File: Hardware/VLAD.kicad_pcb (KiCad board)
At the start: 2 copper layers, 90 x 80 mm, 100 parts, among them J1 BMP388, J2 BNO055, J3 Micro_SD_Card, J4 Conn_01x02_Male, J5 Conn_01x03_Male, J6 Conn_01x02_Male, P1 USB_C_Plug_USB2.0, Q1 MMDT2222A, Q2 MMDT2222A, Q3 S8550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

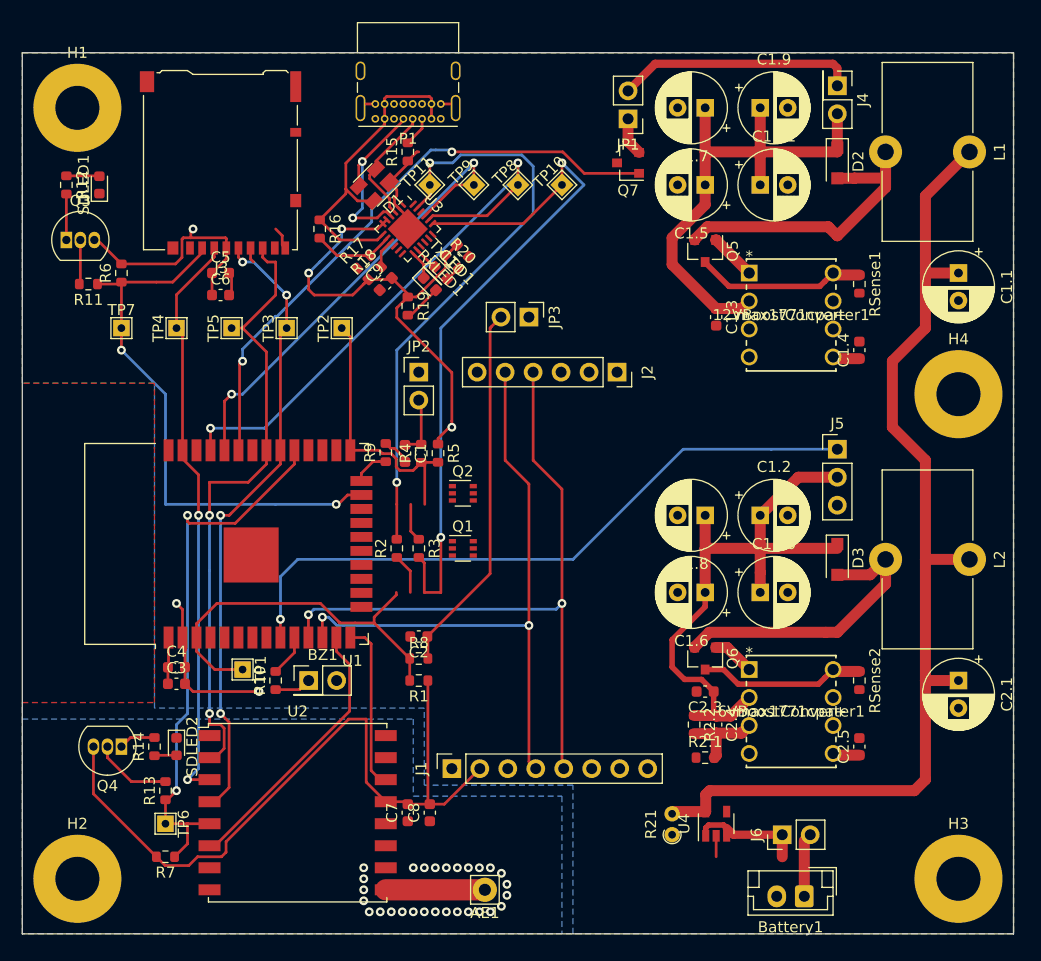
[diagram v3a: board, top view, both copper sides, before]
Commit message: Executive decision to use THT capacitors
THT >>>>>>>>>>>> SMD
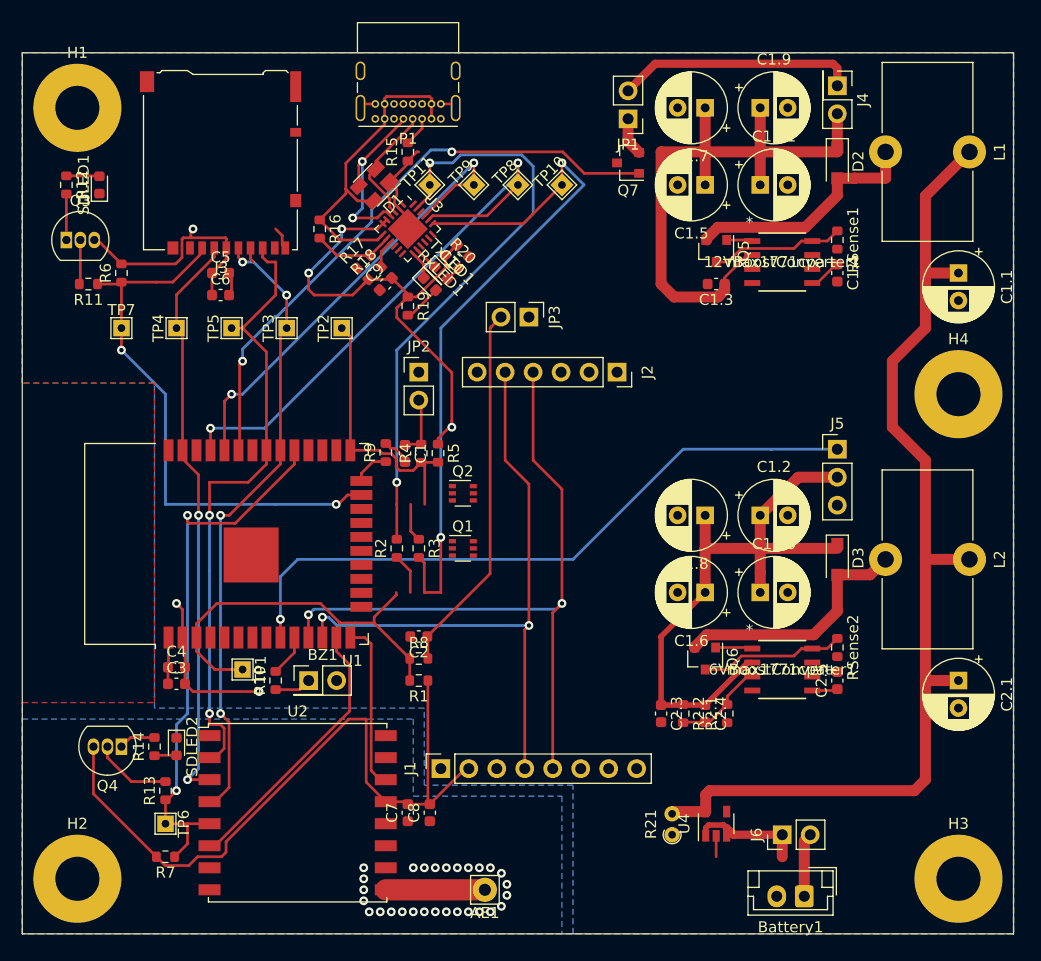
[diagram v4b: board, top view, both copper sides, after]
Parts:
- 12VBoostConverter1, 6VBoostConverter1: footprint footprints:max1771cpa&plus_ -> iclr:MAX1771CSA&plus_
- moved C1.4 7.28 mm to (94.0, 40.0), turned to 270 degrees
- moved C2.5 6.32 mm to (94.0, 77.0)
- moved C2.3 4.47 mm to (78.0, 80.0), turned to 270 degrees
- moved R2.1 4.47 mm to (84.0, 80.0), turned to 90 degrees
- moved RSense1 4.47 mm to (94.0, 37.0)
- moved RSense2 3.61 mm to (94.0, 74.0)
- moved 12VBoostConverter1 3.16 mm to (89.0, 39.0)
- moved 6VBoostConverter1 3.00 mm to (89.0, 76.0)
- moved C1.3 3.00 mm to (83.0, 41.0), turned to 180 degrees
- moved C2.4 1.41 mm to (82.0, 80.0)
- moved R2.2 1.41 mm to (80.0, 80.0)
- moved J1 1.00 mm to (58.0, 85.0)
- moved Q5 1.00 mm to (83.0, 38.0)
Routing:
- net +12V: track 46.9 -> 56.5 mm
- net Net-(D2-Pad2): track 27.6 -> 22.0 mm
- net Net-(D3-Pad2): track 26.9 -> 22.6 mm
- net Net-(12VBoostConverter1-Pad8): track 15.5 -> 12.2 mm
- net Net-(6VBoostConverter1-Pad8): track 15.2 -> 13.2 mm
- net Net-(12VBoostConverter1-Pad1): track 4.29 -> 2.37 mm
- net +6V: track 55.2 -> 56.2 mm
- net +3V3: track 150.0 -> 149.0 mm
- net Net-(12VBoostConverter1-Pad5): track 2.44 -> 2.97 mm
- net Net-(6VBoostConverter1-Pad1): track 3.88 -> 3.37 mm

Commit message: Traccs done, meme time
Need to fix the silkscreen stuff for the components and also the back silkscreen memes etc.
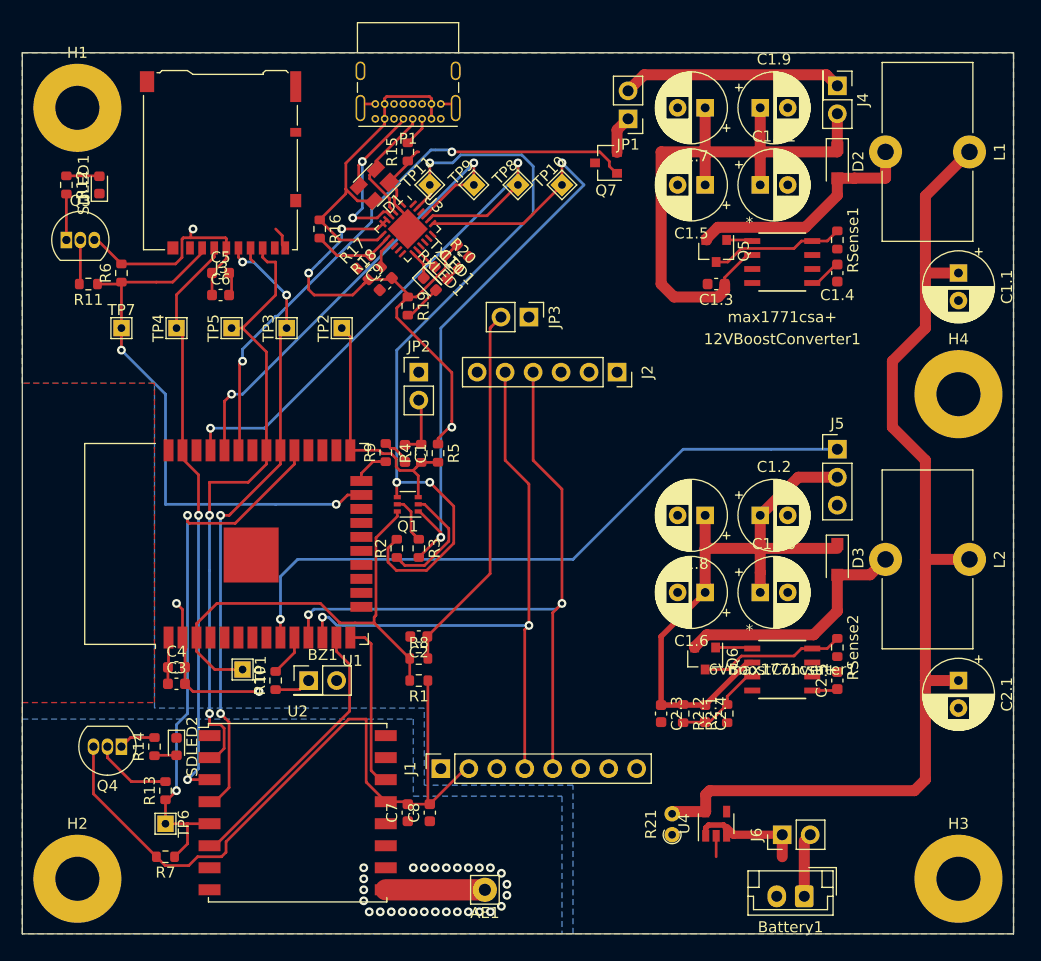
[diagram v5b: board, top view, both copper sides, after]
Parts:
- removed Q2: MMDT2222A, Package_TO_SOT_SMD:SOT-363_SC-70-6
- 12VBoostConverter1, 6VBoostConverter1: value max1771cpa+ -> max1771csa+
- moved Q1 6.40 mm to (55.0, 61.0), turned to 180 degrees
- moved Q7 2.00 mm to (73.0, 30.0)
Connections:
- Q1 pad 1: /EN -> /USB_RTS
- Q1 pad 3: (no net) -> /IO0
- Q1 pad 4: (no net) -> /USB_DTR
- Q1 pad 5: (no net) -> Net-(Q1-Pad5)
- Q1 pad 6: /USB_RTS -> /EN
- R3 pad 1: Net-(Q2-Pad2) -> Net-(Q1-Pad5)
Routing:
- net /USB_DTR: track 53.7 -> 69.0 mm, vias 2 -> 3
- net /EN: track 36.1 -> 43.5 mm
- net Net-(Q1-Pad2): track 3.68 -> 10.8 mm
- net Net-(Q1-Pad5): track 0.00 -> 4.32 mm
- net /USB_RTS: track 65.3 -> 61.4 mm
- net Net-(Q2-Pad2): track 3.48 -> 0.00 mm
- net Net-(J4-Pad1): track 21.8 -> 20.0 mm
- net 12VBusSwitch: track 54.3 -> 52.6 mm
- net /IO0: track 25.1 -> 23.8 mm

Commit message: Added Silkscreens
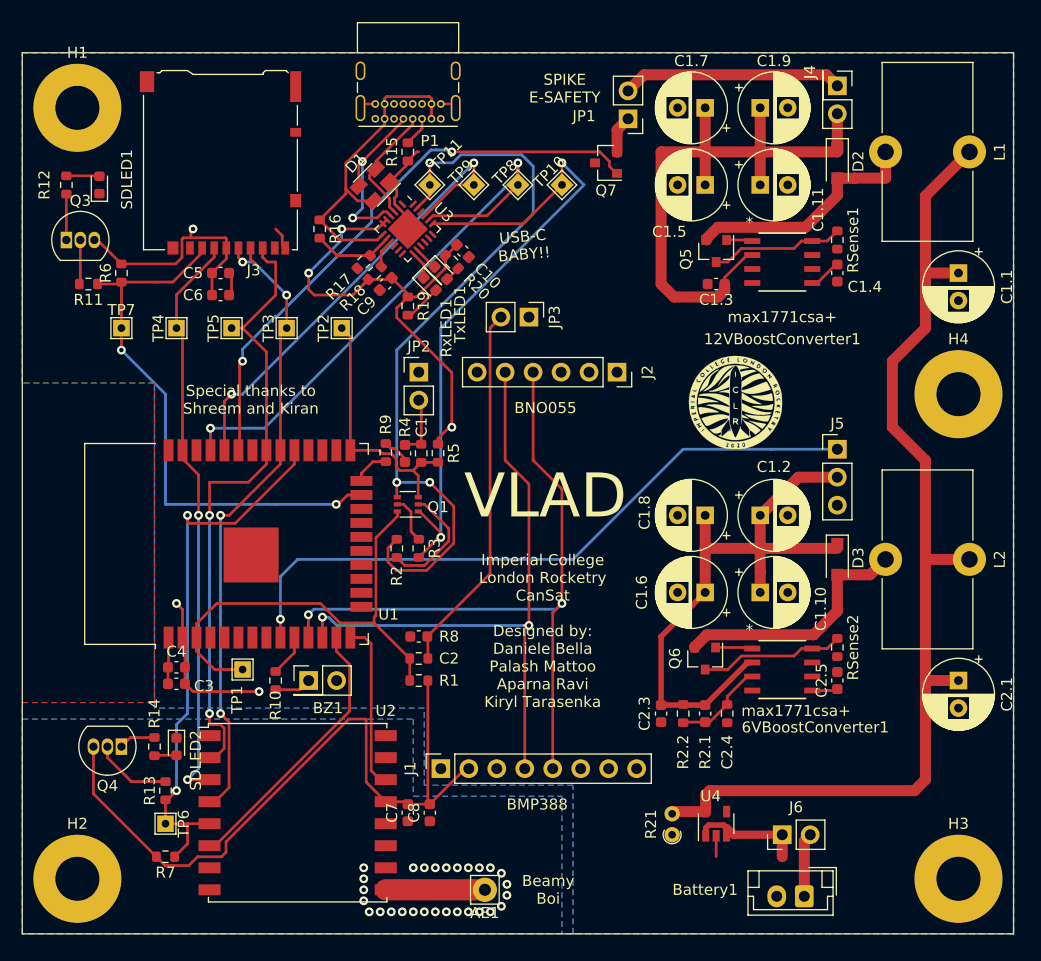
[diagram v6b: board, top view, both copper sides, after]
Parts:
- added G***: LOGO, iclr:iclr_logo, B.Cu at (26.2, 72.0)
- added G***: LOGO, iclr:iclr_logo, F.Cu at (84.8, 51.8)
- added G***: LOGO, iclr:VLAD, B.Cu at (87.0, 60.0)
- added REF**: Write_Pad, iclr:Write_Pad, F.Cu at (26.0, 57.2)
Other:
- board text added: "BMP388"
- board text added: "BNO055"
- board text added: "Beamy Boi"
- board text added: "Imperial College London Rocketry CanSat Designed by: Daniele Bella Palash Mattoo Aparna Ravi Kiryl Tarasenka"
- board text added: "SPIKE E-SAFETY"
- board text added: "Special thanks to Shreem and Kiran"
- board text added: "USB-C BABY!!"
- board text added: "VLAD"
- board text added: "Very Long And Deadly 2020/2021 Imperial College London Rocketry Tinned Soup Satellite Lead by Palash Mattoo The Gardeners: Yasmine Chan Victor Moanta Aparna Ravi Nadja Radjovic Kiryl Tarasenka Daniele Bella"
